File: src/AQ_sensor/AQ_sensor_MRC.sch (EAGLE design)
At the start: 50 parts, among them IC2 MCP73831/OT, J1 F-1X03-SIP-100-32, SW1 PCM12SMTR, SW2 PCM12SMTR, U2 TEXAS_INSTRUMENTS_SN74HC125TE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, U3 TEXAS_INSTRUMENTS_LM1117IMP-3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, X1 53048-08, X2 SIMLOCK-C707_10M006_512_2, X4 50 Ohms

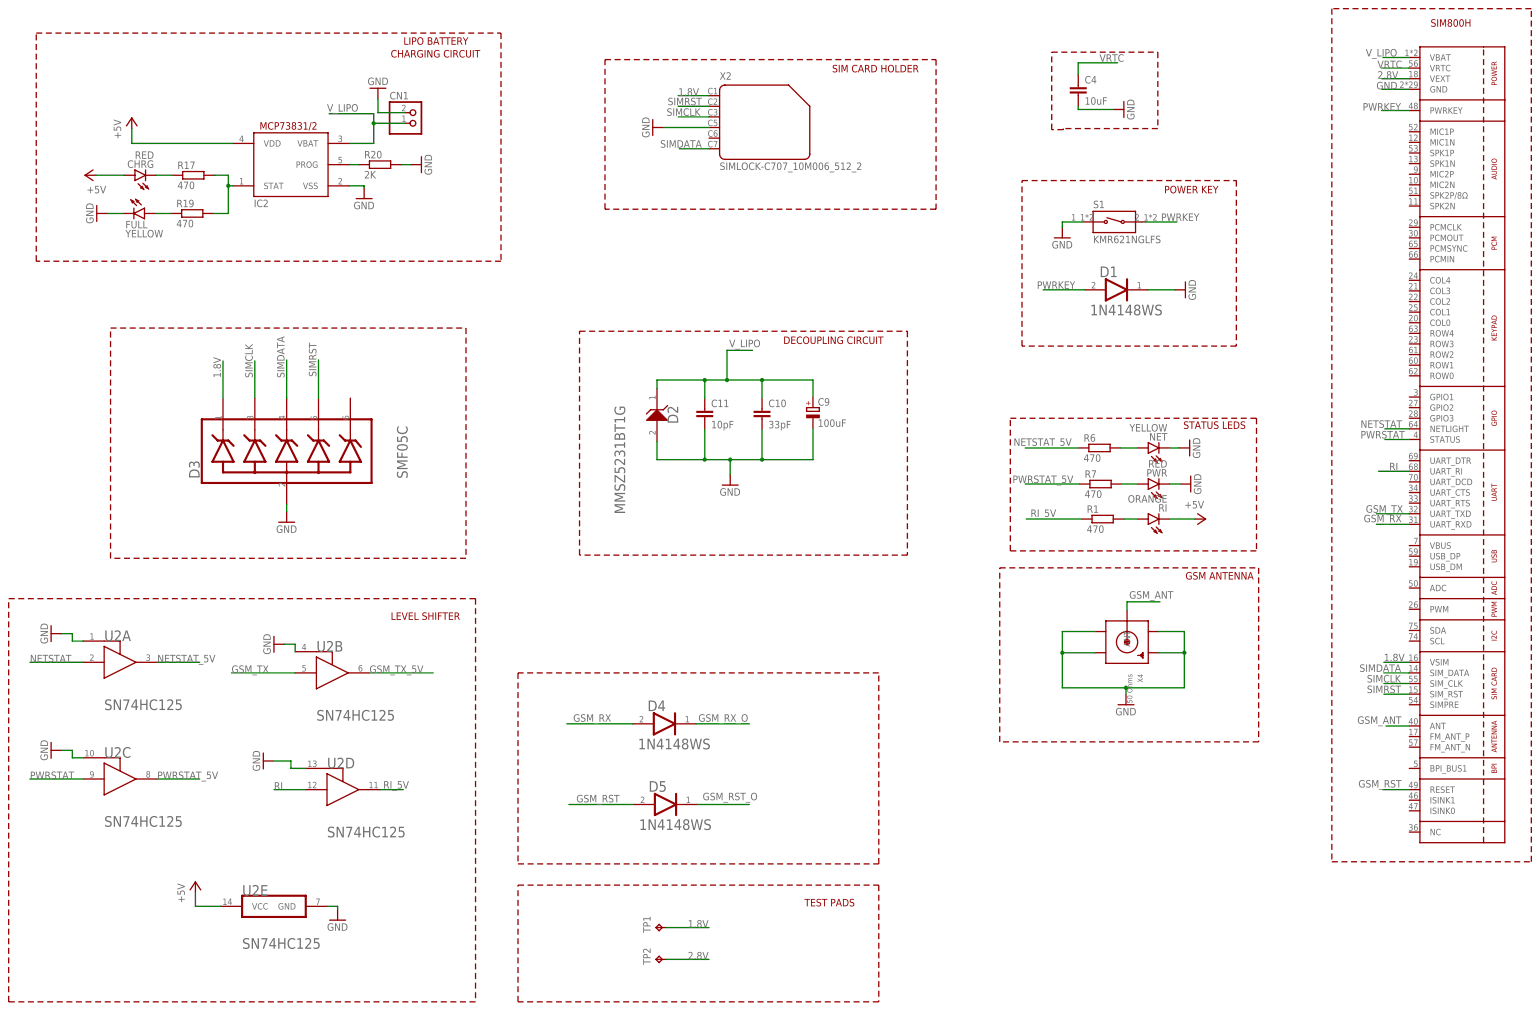
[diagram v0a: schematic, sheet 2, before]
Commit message: Added Managed library to design
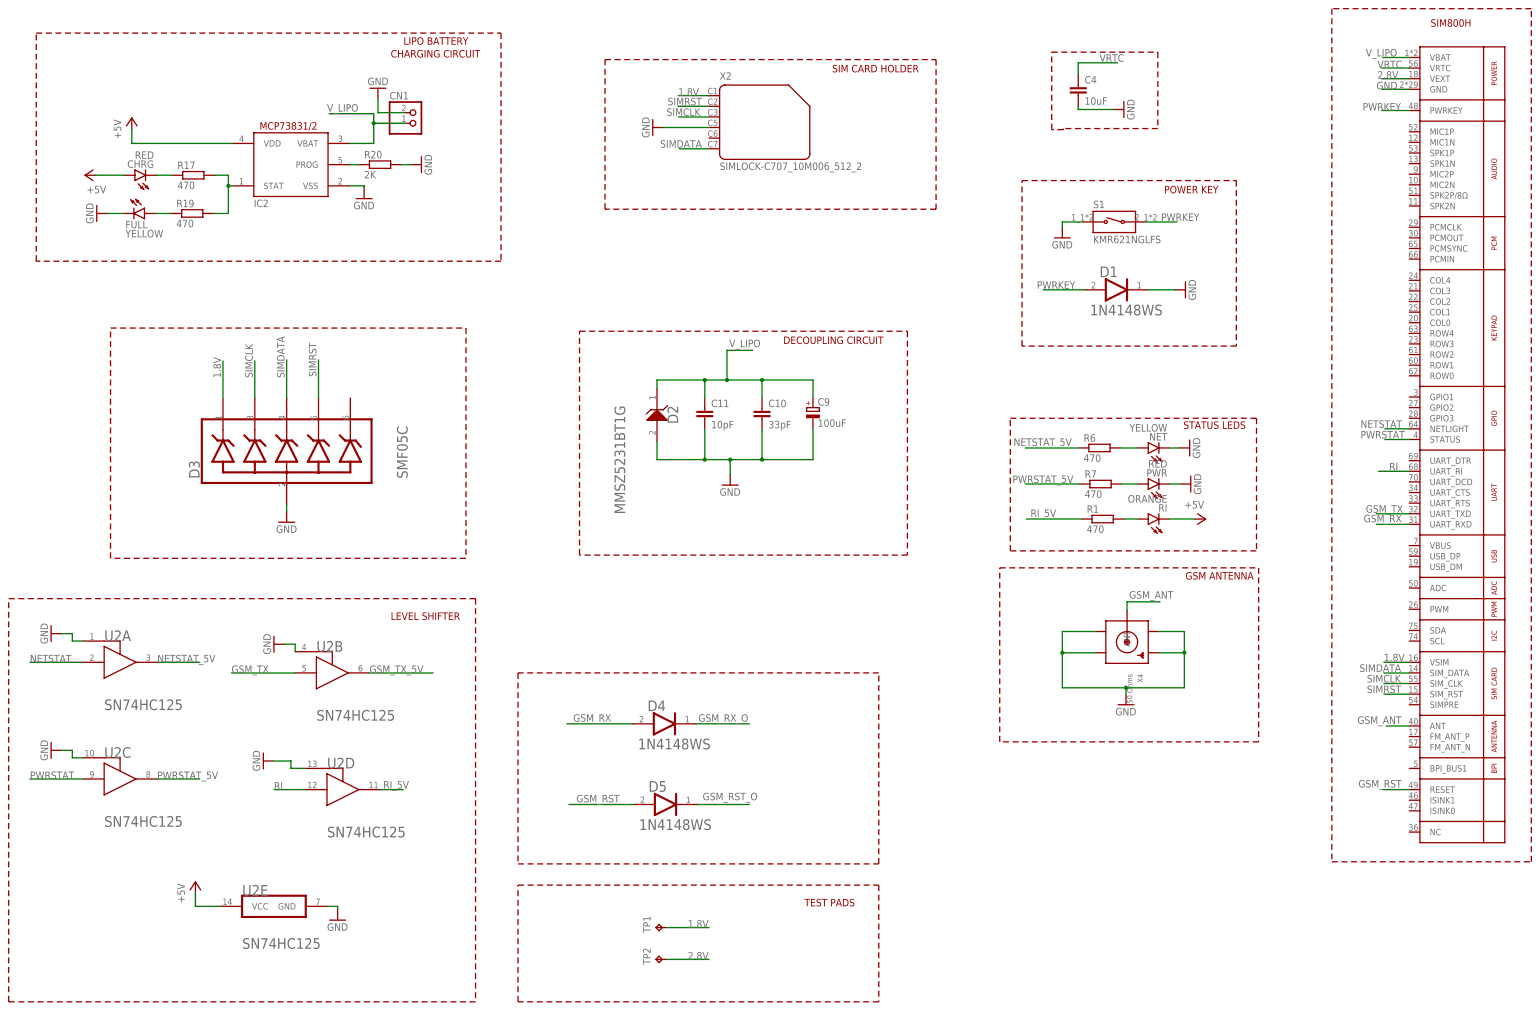
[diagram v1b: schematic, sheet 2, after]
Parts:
- CN1: device AQ_sensor_WB_KE_KNBS:JST_2PIN-SMT-RA -> AQ_sensor_MRC:JST_2PIN-SMT-RA
- D1, D4, D5: device ON Semi - 1N4148WS:ON_SEMI_1N4148WSON_SEMI_1N4148WS_0_0 -> AQ_sensor_MRC:ON_SEMI_1N4148WSON_SEMI_1N4148WS_0_0
- D2: device On Semiconductor - MMSZ5231BT1G:ON_SEMICONDUCTOR_MMSZ5231BT1GON_SEMICONDUCTOR_MMSZ5231BT1G_0_0 -> AQ_sensor_MRC:ON_SEMICONDUCTOR_MMSZ5231BT1GON_SEMICONDUCTOR_MMSZ5231BT1G_0_0
- D3: device Semtech - SMF05C:SEMTECH_SMF05CSEMTECH_SMF05C_0_0 -> AQ_sensor_MRC:SEMTECH_SMF05CSEMTECH_SMF05C_0_0
- H1, H2, H3, H4: device AQ_sensor_WB_KE_KNBS:MOUNT-PAD-ROUND2.8 -> AQ_sensor_MRC:MOUNT-PAD-ROUND2.8
- IC2: device adafruit:MCP73831/OT -> AQ_sensor_MRC:MCP73831/OT
- J1: device AQ_sensor_WB_KE_KNBS:F-1X03-SIP-100-32 -> AQ_sensor_MRC:F-1X03-SIP-100-32
- MICRO_USB: device AQ_sensor_WB_KE_KNBS:10118192-0001LF -> AQ_sensor_MRC:10118192-0001LF
- S1: device KMR621NGLFS:KMR621NGLFS -> AQ_sensor_MRC:KMR621NGLFS
- SV1, SV2: device AQ_sensor_WB_KE_KNBS:FE15-1 -> AQ_sensor_MRC:FE15-1
- SW1, SW2: device AQ_sensor_WB_KE_KNBS:PCM12SMTR -> AQ_sensor_MRC:PCM12SMTR
- U1: device adafruit:GSM_SIM800L -> AQ_sensor_MRC:GSM_SIM800L
- U2: device Texas Instruments - SN74HC125:TEXAS_INSTRUMENTS_SN74HC125TEXAS_INSTRUMENTS_SN74HC125_0_0 -> AQ_sensor_MRC:TEXAS_INSTRUMENTS_SN74HC125TEXAS_INSTRUMENTS_SN74HC125_0_0
- U3: device AQ_sensor_WB_KE_KNBS:TEXAS_INSTRUMENTS_LM1117IMP-3.3-NOPBTEXAS_INSTRUMENTS_LM1117IMP-3.3-NOPB_0_0 -> AQ_sensor_MRC:TEXAS_INSTRUMENTS_LM1117IMP-3.3-NOPBTEXAS_INSTRUMENTS_LM1117IMP-3.3-NOPB_0_0
- X1: device AQ_sensor_WB_KE_KNBS:53048-08 -> AQ_sensor_MRC:53048-08
- X2: device con-amphenol:SIMLOCK-C707_10M006_512_2 -> AQ_sensor_MRC:SIMLOCK-C707_10M006_512_2
- X4: device adafruit:SMACONNECTOR_EDGE_UFL -> AQ_sensor_MRC:SMACONNECTOR_EDGE_UFL

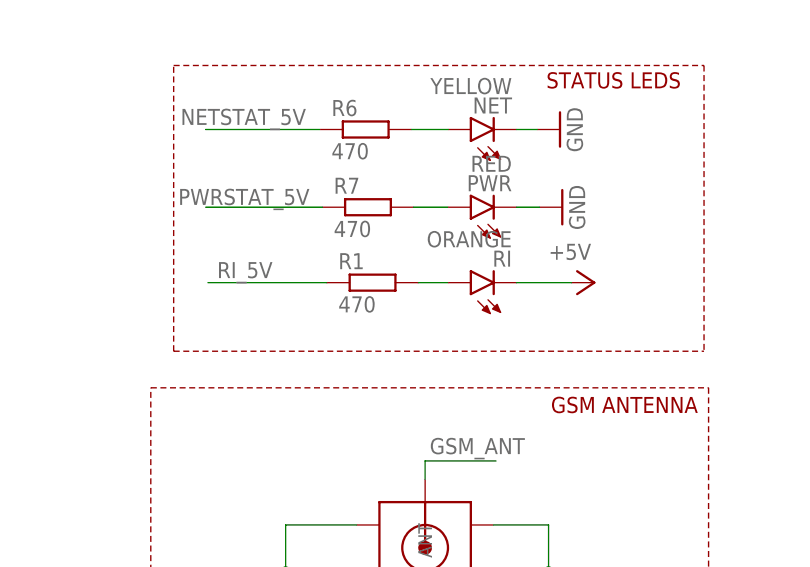
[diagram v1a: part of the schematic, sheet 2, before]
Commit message: Modifed RI LED connection
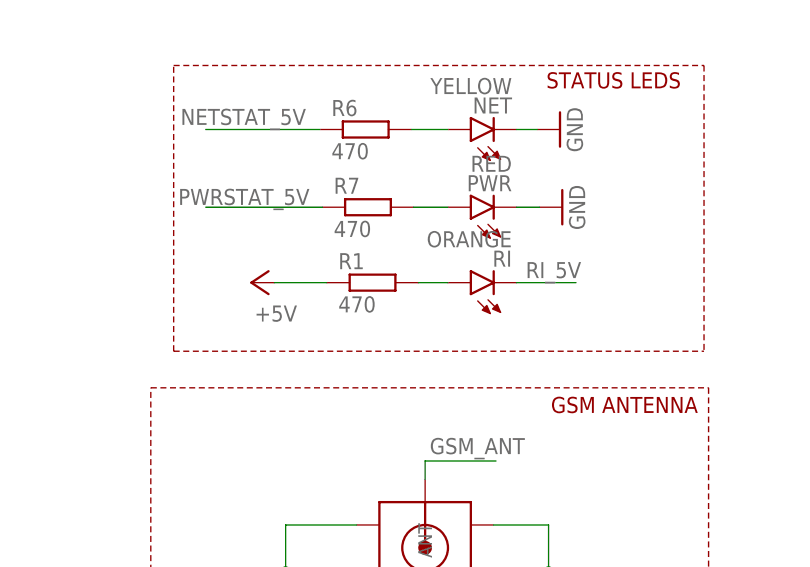
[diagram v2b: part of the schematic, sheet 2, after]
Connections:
- net +5V: now also R1.1; no longer RI.C
- net RI_5V: now also RI.C; no longer R1.1
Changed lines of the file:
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@@
 <setting verticaltext="up"/>
 </settings>
-<grid distance="0.1" unitdist="inch" unit="inch" style="lines" multiple="1" display="no" altdistance="0.01" altunitdist="inch" altunit="inch"/>
+<grid distance="0.01" unitdist="inch" unit="inch" style="dots" multiple="1" display="yes" altdistance="0.01" altunitdist="inch" altunit="inch"/>
 <layers>
 <layer number="1" name="Top" color="4" fill="1" visible="no" active="no"/>
@@
 <attribute name="VALUE" x="290.068" y="128.905" size="1.778" layer="96" rot="R180"/>
 </instance>
-<instance part="P+8" gate="1" x="299.212" y="123.19" smashed="yes" rot="R270">
-<attribute name="VALUE" x="294.132" y="125.73" size="1.778" layer="96"/>
+<instance part="P+8" gate="1" x="261.112" y="123.19" smashed="yes" rot="R90">
+<attribute name="VALUE" x="266.192" y="120.65" size="1.778" layer="96" rot="R180"/>
 </instance>
 </instances>
@@
 </segment>
 <segment>
-<pinref part="RI" gate="G$1" pin="C"/>
 <pinref part="P+8" gate="1" pin="+5V"/>
-<wire x1="290.576" y1="123.19" x2="296.672" y2="123.19" width="0.1524" layer="91"/>
+<pinref part="R1" gate="G$1" pin="1"/>
+<wire x1="263.652" y1="123.19" x2="269.494" y2="123.19" width="0.1524" layer="91"/>
 </segment>
 </net>
@@
 </segment>
 <segment>
-<pinref part="R1" gate="G$1" pin="1"/>
-<wire x1="269.494" y1="123.19" x2="256.286" y2="123.19" width="0.1524" layer="91"/>
-<label x="257.302" y="123.698" size="1.778" layer="95"/>
-</segment>
-</net>
+<pinref part="RI" gate="G$1" pin="C"/>
+<wire x1="290.576" y1="123.19" x2="297.18" y2="123.19" width="0.1524" layer="91"/>
+<label x="291.592" y="123.698" size="1.778" layer="95"/>
+</segment>
+</net>
